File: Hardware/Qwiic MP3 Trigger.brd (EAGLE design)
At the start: 25.4 x 50.8 mm, 99 parts, among them J1 MICRO-SD, J3 PTH, J7 ISP, J8 3.5mm Audio, J9 Poke-Home, U1 TPA2005D1, U2 WT2003S, U3 AP2112-3.3V, U4 ATTINY84-ARDUINO

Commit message: File name clean up.
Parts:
- removed U$1: SPARKX-LOGO3, SparkX:SPARKX-SMALL
- removed U$2: SPARKX-LOGO4, SparkX:SPARKX-MEDIUM
- removed U$23: (no value), buzzard_labels (17):QWIIC_MP32
- added LOGO2: SFE_LOGO_NAME.1_INCH, SparkFun-Aesthetics:SFE_LOGO_NAME_.1
- added LOGO3: SFE_LOGO_NAME_FLAME.1_INCH, SparkFun-Aesthetics:SFE_LOGO_NAME_FLAME_.1
- added U$51: (no value), buzzard_labels (1):MP32
- added U$53: (no value), buzzard_labels (1):QWIIC1
- moved U$24 9.28 mm to (15.0, 32.5)
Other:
- board text added: "V10"
- board text removed: "X02"

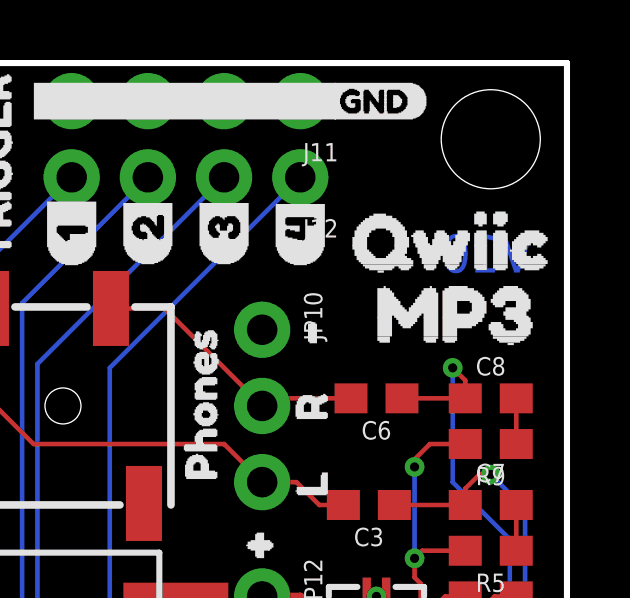
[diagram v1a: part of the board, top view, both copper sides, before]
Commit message: Fixing product name silk. Adding production panel.
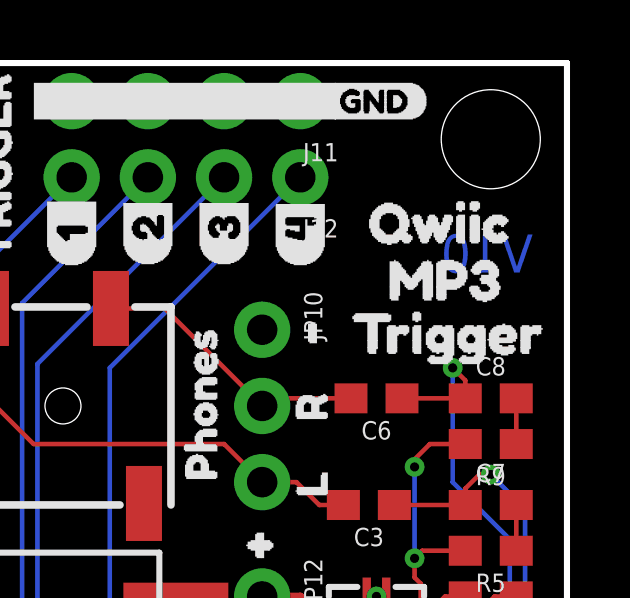
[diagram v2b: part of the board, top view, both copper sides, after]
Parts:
- removed U$51: (no value), buzzard_labels (1):MP32
- removed U$53: (no value), buzzard_labels (1):QWIIC1
- added U$1: (no value), buzzard_labels (3):MP31
- added U$23: (no value), buzzard_labels (3):QWIIC0
- added U$49: (no value), buzzard_labels (2):TRIGGER4
- added U$50: (no value), buzzard_labels (3):TRIGGER2
- moved LOGO3 1.27 mm to (6.86, 36.3)
- moved U$24 1.27 mm to (15.0, 33.8)
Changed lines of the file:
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@@
 <layer number="23" name="tOrigins" color="15" fill="1" visible="yes" active="yes"/>
 <layer number="24" name="bOrigins" color="15" fill="1" visible="yes" active="yes"/>
-<layer number="25" name="tNames" color="7" fill="1" visible="yes" active="yes"/>
-<layer number="26" name="bNames" color="7" fill="1" visible="yes" active="yes"/>
-<layer number="27" name="tValues" color="7" fill="1" visible="yes" active="yes"/>
-<layer number="28" name="bValues" color="7" fill="1" visible="yes" active="yes"/>
-<layer number="29" name="tStop" color="7" fill="3" visible="yes" active="yes"/>
-<layer number="30" name="bStop" color="7" fill="6" visible="yes" active="yes"/>
-<layer number="31" name="tCream" color="7" fill="4" visible="yes" active="yes"/>
-<layer number="32" name="bCream" color="7" fill="5" visible="yes" active="yes"/>
-<layer number="33" name="tFinish" color="6" fill="3" visible="yes" active="yes"/>
-<layer number="34" name="bFinish" color="6" fill="6" visible="yes" active="yes"/>
-<layer number="35" name="tGlue" color="7" fill="4" visible="yes" active="yes"/>
-<layer number="36" name="bGlue" color="7" fill="5" visible="yes" active="yes"/>
-<layer number="37" name="tTest" color="7" fill="1" visible="yes" active="yes"/>
-<layer number="38" name="bTest" color="7" fill="1" visible="yes" active="yes"/>
-<layer number="39" name="tKeepout" color="4" fill="11" visible="yes" active="yes"/>
-<layer number="40" name="bKeepout" color="1" fill="11" visible="yes" active="yes"/>
-<layer number="41" name="tRestrict" color="4" fill="10" visible="yes" active="yes"/>
-<layer number="42" name="bRestrict" color="1" fill="10" visible="yes" active="yes"/>
-<layer number="43" name="vRestrict" color="2" fill="10" visible="yes" active="yes"/>
-<layer number="44" name="Drills" color="7" fill="1" visible="yes" active="yes"/>
+<layer number="25" name="tNames" color="7" fill="1" visible="no" active="yes"/>
+<layer number="26" name="bNames" color="7" fill="1" visible="no" active="yes"/>
+<layer number="27" name="tValues" color="7" fill="1" visible="no" active="yes"/>
+<layer number="28" name="bValues" color="7" fill="1" visible="no" active="yes"/>
+<layer number="29" name="tStop" color="7" fill="3" visible="no" active="yes"/>
+<layer number="30" name="bStop" color="7" fill="6" visible="no" active="yes"/>
+<layer number="31" name="tCream" color="7" fill="4" visible="no" active="yes"/>
+<layer number="32" name="bCream" color="7" fill="5" visible="no" active="yes"/>
+<layer number="33" name="tFinish" color="6" fill="3" visible="no" active="yes"/>
+<layer number="34" name="bFinish" color="6" fill="6" visible="no" active="yes"/>
+<layer number="35" name="tGlue" color="7" fill="4" visible="no" active="yes"/>
+<layer number="36" name="bGlue" color="7" fill="5" visible="no" active="yes"/>
+<layer number="37" name="tTest" color="7" fill="1" visible="no" active="yes"/>
+<layer number="38" name="bTest" color="7" fill="1" visible="no" active="yes"/>
+<layer number="39" name="tKeepout" color="4" fill="11" visible="no" active="yes"/>
+<layer number="40" name="bKeepout" color="1" fill="11" visible="no" active="yes"/>
+<layer number="41" name="tRestrict" color="4" fill="10" visible="no" active="yes"/>
+<layer number="42" name="bRestrict" color="1" fill="10" visible="no" active="yes"/>
+<layer number="43" name="vRestrict" color="2" fill="10" visible="no" active="yes"/>
+<layer number="44" name="Drills" color="7" fill="1" visible="no" active="yes"/>
 <layer number="45" name="Holes" color="7" fill="1" visible="yes" active="yes"/>
 <layer number="46" name="Milling" color="3" fill="1" visible="yes" active="yes"/>
-<layer number="47" name="Measures" color="7" fill="1" visible="yes" active="yes"/>
-<layer number="48" name="Document" color="7" fill="1" visible="yes" active="yes"/>
-<layer number="49" name="Reference" color="7" fill="1" visible="yes" active="yes"/>
-<layer number="50" name="dxf" color="7" fill="1" visible="yes" active="yes"/>
+<layer number="47" name="Measures" color="7" fill="1" visible="no" active="yes"/>
+<layer number="48" name="Document" color="7" fill="1" visible="no" active="yes"/>
+<layer number="49" name="Reference" color="7" fill="1" visible="no" active="yes"/>
+<layer number="50" name="dxf" color="7" fill="1" visible="no" active="yes"/>
 <layer number="51" name="tDocu" color="6" fill="1" visible="yes" active="yes"/>
-<layer number="52" name="bDocu" color="7" fill="1" visible="yes" active="yes"/>
+<layer number="52" name="bDocu" color="7" fill="1" visible="no" active="yes"/>
 <layer number="91" name="Nets" color="2" fill="1" visible="no" active="no"/>
 <layer number="92" name="Busses" color="1" fill="1" visible="no" active="no"/>
@@
 <element name="U$15" library="buzzard_labels (17)" package="PHONES0" value="" x="13.208" y="35.814" smashed="yes" rot="R90"/>
 <element name="U$20" library="buzzard_labels (17)" package="SPEAKER1" value="" x="0.381" y="25.4" smashed="yes"/>
-<element name="U$24" library="buzzard_labels (17)" package="QWIIC_MP32" value="" x="14.986" y="32.512" smashed="yes" rot="MR0"/>
+<element name="U$24" library="buzzard_labels (17)" package="QWIIC_MP32" value="" x="14.986" y="33.782" smashed="yes" rot="MR0"/>
 <element name="U$25" library="buzzard_labels (16)" package="#6" value="" x="17.399" y="28.829" smashed="yes" rot="MR90"/>
 <element name="U$28" library="buzzard_labels (16)" package="#5" value="" x="17.145" y="31.496" smashed="yes" rot="MR90"/>
@@
 </element>
 <element name="LOGO2" library="SparkFun-Aesthetics" package="SFE_LOGO_NAME_.1" value="SFE_LOGO_NAME.1_INCH" x="12.7" y="13.97" smashed="yes"/>
-<element name="LOGO3" library="SparkFun-Aesthetics" package="SFE_LOGO_NAME_FLAME_.1" value="SFE_LOGO_NAME_FLAME.1_INCH" x="6.858" y="35.052" smashed="yes" rot="MR0"/>
-<element name="U$51" library="buzzard_labels (1)" package="MP32" value="" x="17.399" y="42.418" smashed="yes"/>
-<element name="U$53" library="buzzard_labels (1)" package="QWIIC1" value="" x="16.637" y="44.831" smashed="yes"/>
+<element name="LOGO3" library="SparkFun-Aesthetics" package="SFE_LOGO_NAME_FLAME_.1" value="SFE_LOGO_NAME_FLAME.1_INCH" x="6.858" y="36.322" smashed="yes" rot="MR0"/>
+<element name="U$49" library="buzzard_labels (2)" package="TRIGGER4" value="" x="12.827" y="31.242" smashed="yes" rot="MR0"/>
+<element name="U$1" library="buzzard_labels (3)" package="MP31" value="" x="18.288" y="43.561" smashed="yes"/>
+<element name="U$23" library="buzzard_labels (3)" package="QWIIC0" value="" x="17.653" y="45.466" smashed="yes"/>
+<element name="U$50" library="buzzard_labels (3)" package="TRIGGER2" value="" x="17.145" y="41.783" smashed="yes"/>
 </elements>
 <signals>

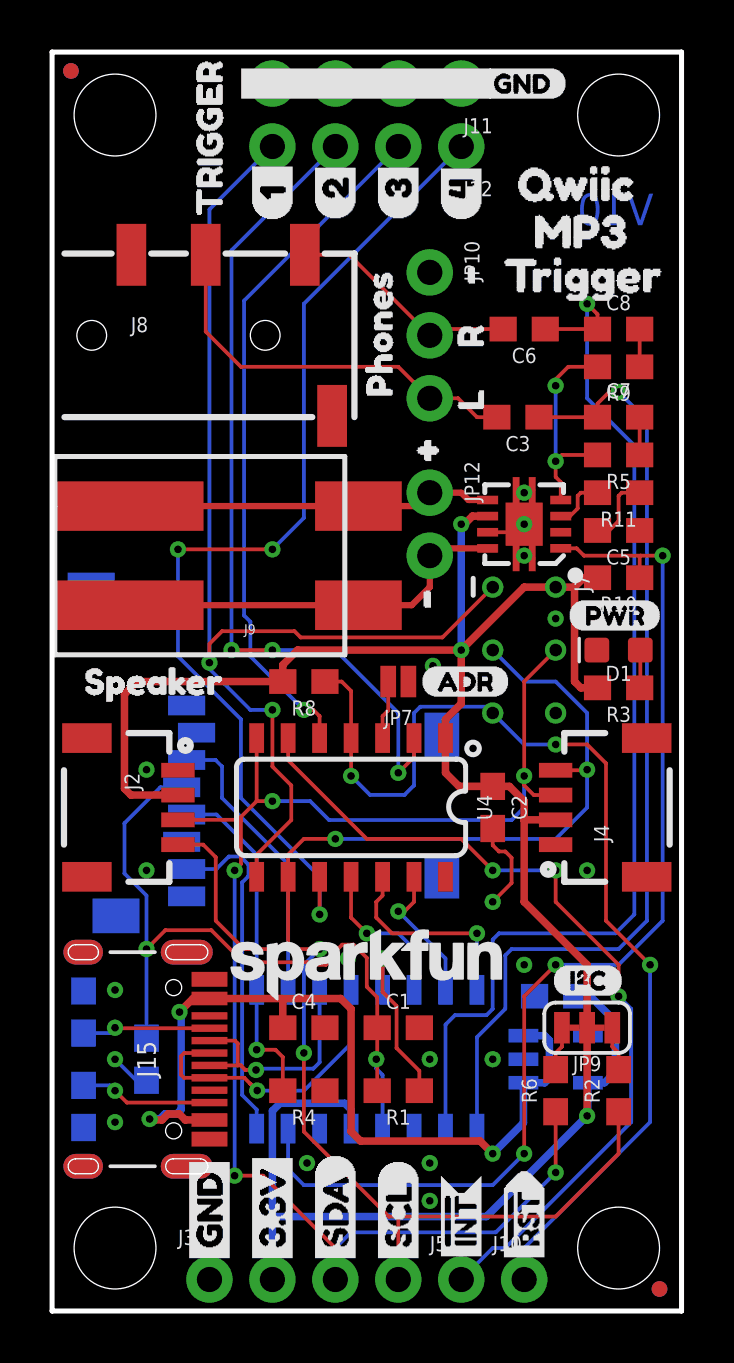
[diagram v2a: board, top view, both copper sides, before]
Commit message: Routing Playing pin on WS to Shutdown pin on amp
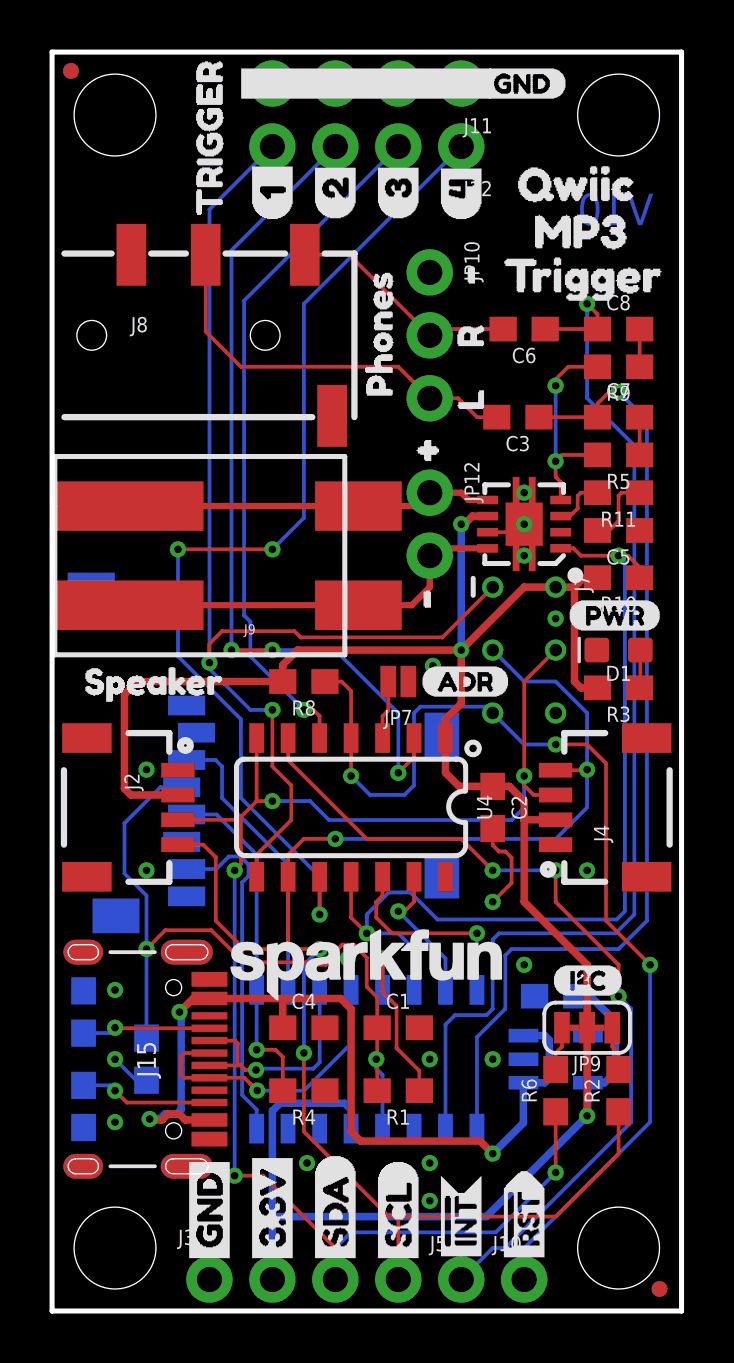
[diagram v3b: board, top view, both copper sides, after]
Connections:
- net !SDN: no longer R10.1, U1.1
- net PLAYING: now also R10.1, U1.1
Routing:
- net !SDN: track 45.0 -> 0.00 mm, vias 3 -> 0
- net PLAYING: track 6.36 -> 36.9 mm, vias 1 -> 2
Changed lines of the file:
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@@
 <layer number="44" name="Drills" color="7" fill="1" visible="no" active="yes"/>
 <layer number="45" name="Holes" color="7" fill="1" visible="yes" active="yes"/>
-<layer number="46" name="Milling" color="3" fill="1" visible="yes" active="yes"/>
+<layer number="46" name="Milling" color="3" fill="1" visible="no" active="yes"/>
 <layer number="47" name="Measures" color="7" fill="1" visible="no" active="yes"/>
 <layer number="48" name="Document" color="7" fill="1" visible="no" active="yes"/>
@@
 <layer number="95" name="Names" color="7" fill="1" visible="no" active="no"/>
 <layer number="96" name="Values" color="7" fill="1" visible="no" active="no"/>
-<layer number="2" name="Route2" color="1" fill="3" visible="yes" active="yes"/>
-<layer number="15" name="Route15" color="4" fill="6" visible="yes" active="yes"/>
+<layer number="2" name="Route2" color="1" fill="3" visible="no" active="yes"/>
+<layer number="15" name="Route15" color="4" fill="6" visible="no" active="yes"/>
 <layer number="3" name="Route3" color="4" fill="3" visible="no" active="no"/>
 <layer number="4" name="Route4" color="1" fill="4" visible="no" active="no"/>
@@
 </signal>
 <signal name="!SDN">
-<contactref element="R10" pad="1"/>
-<contactref element="U1" pad="1"/>
 <contactref element="U2" pad="7"/>
-<wire x1="9.525" y1="7.36" x2="9.525" y2="5.715" width="0.1524" layer="16"/>
-<wire x1="9.525" y1="5.715" x2="10.16" y2="5.08" width="0.1524" layer="16"/>
-<wire x1="10.16" y1="5.08" x2="17.78" y2="5.08" width="0.1524" layer="16"/>
-<wire x1="17.78" y1="5.08" x2="19.05" y2="6.35" width="0.1524" layer="16"/>
-<wire x1="20.525" y1="30.775" x2="21.168" y2="30.775" width="0.1524" layer="1"/>
-<wire x1="21.168" y1="30.775" x2="21.463" y2="30.48" width="0.1524" layer="1"/>
-<wire x1="21.463" y1="30.48" x2="23.749" y2="30.48" width="0.1524" layer="1"/>
-<via x="24.638" y="30.48" extent="1-16" drill="0.3048"/>
-<wire x1="23.749" y1="30.48" x2="24.638" y2="30.48" width="0.1524" layer="1"/>
-<wire x1="24.638" y1="30.48" x2="24.638" y2="15.748" width="0.1524" layer="16"/>
-<wire x1="23.71" y1="29.591" x2="23.71" y2="30.441" width="0.1524" layer="1"/>
-<wire x1="23.71" y1="30.441" x2="23.749" y2="30.48" width="0.1524" layer="1"/>
-<via x="19.05" y="6.35" extent="1-16" drill="0.3048"/>
-<wire x1="19.05" y1="6.35" x2="19.05" y2="12.7" width="0.1524" layer="1"/>
-<wire x1="19.05" y1="12.7" x2="20.32" y2="13.97" width="0.1524" layer="1"/>
-<via x="20.32" y="13.97" extent="1-16" drill="0.3048"/>
-<wire x1="20.32" y1="13.97" x2="22.86" y2="13.97" width="0.1524" layer="16"/>
-<wire x1="22.86" y1="13.97" x2="24.638" y2="15.748" width="0.1524" layer="16"/>
 </signal>
 <signal name="IN-AMP">
@@
 <wire x1="12.065" y1="17.52" x2="12.065" y2="15.875" width="0.1524" layer="1"/>
 <wire x1="12.065" y1="15.875" x2="12.7" y2="15.24" width="0.1524" layer="1"/>
+<contactref element="R10" pad="1"/>
+<contactref element="U1" pad="1"/>
+<wire x1="20.525" y1="30.775" x2="21.041" y2="30.775" width="0.1524" layer="1"/>
+<wire x1="21.041" y1="30.775" x2="21.336" y2="30.48" width="0.1524" layer="1"/>
+<wire x1="21.336" y1="30.48" x2="22.86" y2="30.48" width="0.1524" layer="1"/>
+<wire x1="22.86" y1="30.48" x2="23.241" y2="30.48" width="0.1524" layer="1"/>
+<wire x1="23.241" y1="30.48" x2="23.71" y2="30.011" width="0.1524" layer="1"/>
+<wire x1="23.71" y1="30.011" x2="23.71" y2="29.591" width="0.1524" layer="1"/>
+<wire x1="12.7" y1="15.24" x2="12.7" y2="16.002" width="0.1524" layer="16"/>
+<wire x1="12.7" y1="16.002" x2="13.589" y2="16.891" width="0.1524" layer="16"/>
+<wire x1="13.589" y1="16.891" x2="14.4587125" y2="16.891" width="0.1524" layer="16"/>
+<wire x1="14.4587125" y1="16.891" x2="15.5509125" y2="15.7988" width="0.1524" layer="16"/>
+<wire x1="22.7838" y1="15.7988" x2="23.114" y2="16.129" width="0.1524" layer="16"/>
+<wire x1="23.114" y1="16.129" x2="23.114" y2="30.226" width="0.1524" layer="16"/>
+<wire x1="23.114" y1="30.226" x2="22.86" y2="30.48" width="0.1524" layer="16"/>
+<via x="22.86" y="30.48" extent="1-16" drill="0.3048"/>
+<wire x1="15.5509125" y1="15.7988" x2="22.7838" y2="15.7988" width="0.1524" layer="16"/>
 </signal>
 <signal name="MP3-TXO">

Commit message: Rolling to v11 copper
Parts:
- added JP8: INT, SparkFun-Jumpers:SMT-JUMPER_2_NC_TRACE_SILK
- added R7: 10k, SparkFun-Resistors:0603
- JP7: device SparkFun-Jumpers:SMT-JUMPER_2_NO_NO-SILK -> SparkFun-Jumpers:SMT-JUMPER_2_NO_SILK
- moved U$18 0.38 mm to (15.2, 25.4)
- flipped J7 to the bottom
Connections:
- new net N$4: JP8.1, R7.2
- net !INT: now also R7.1
- net 3.3V: now also JP8.2
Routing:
- net !INT: track 34.4 -> 39.5 mm, vias 3 -> 4
- net 3.3V: track 94.7 -> 99.6 mm, vias 3 -> 2
- net N$4: track 0.00 -> 4.09 mm
- net TRIGGER1: track 46.3 -> 48.9 mm, vias 2 -> 3
- net !RST: track 43.0 -> 41.1 mm, vias 3 -> 2
- net SCL: track 62.6 -> 60.8 mm
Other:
- board text added: "V11"
- board text removed: "V10"
